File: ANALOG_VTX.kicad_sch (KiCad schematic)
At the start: 13 parts, among them U13 AT7456ELAH, U8 ZX-SH1.0-3PWT, U9 ZX-SH1.0-4PWT, Y2 XL2EL89COI-111YLC-27M

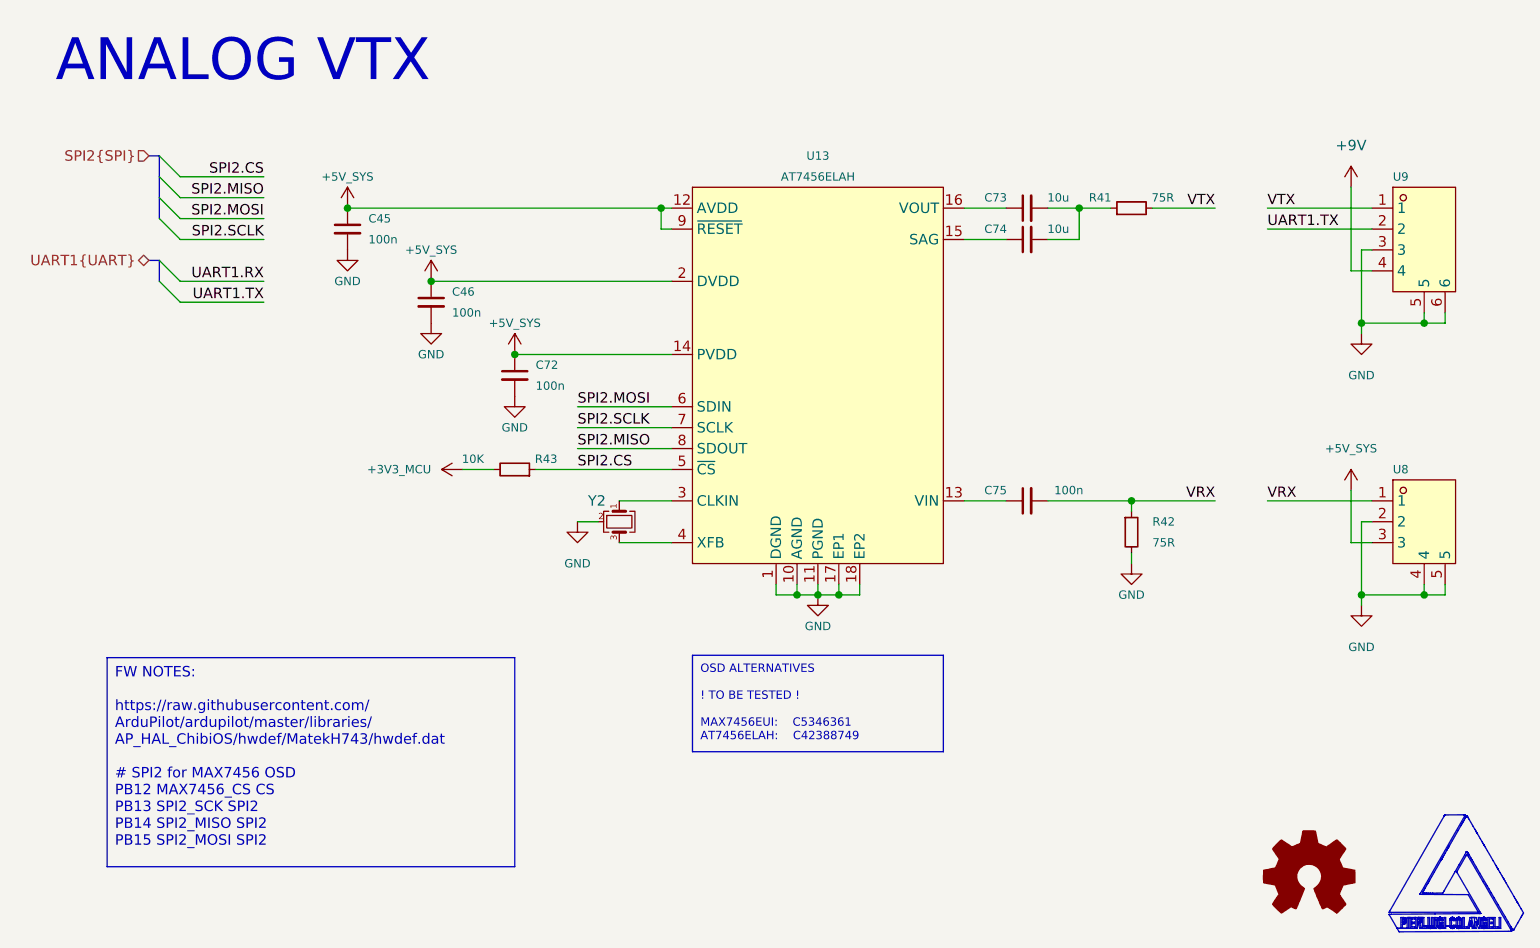
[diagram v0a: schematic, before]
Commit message: grouped ICs and passives
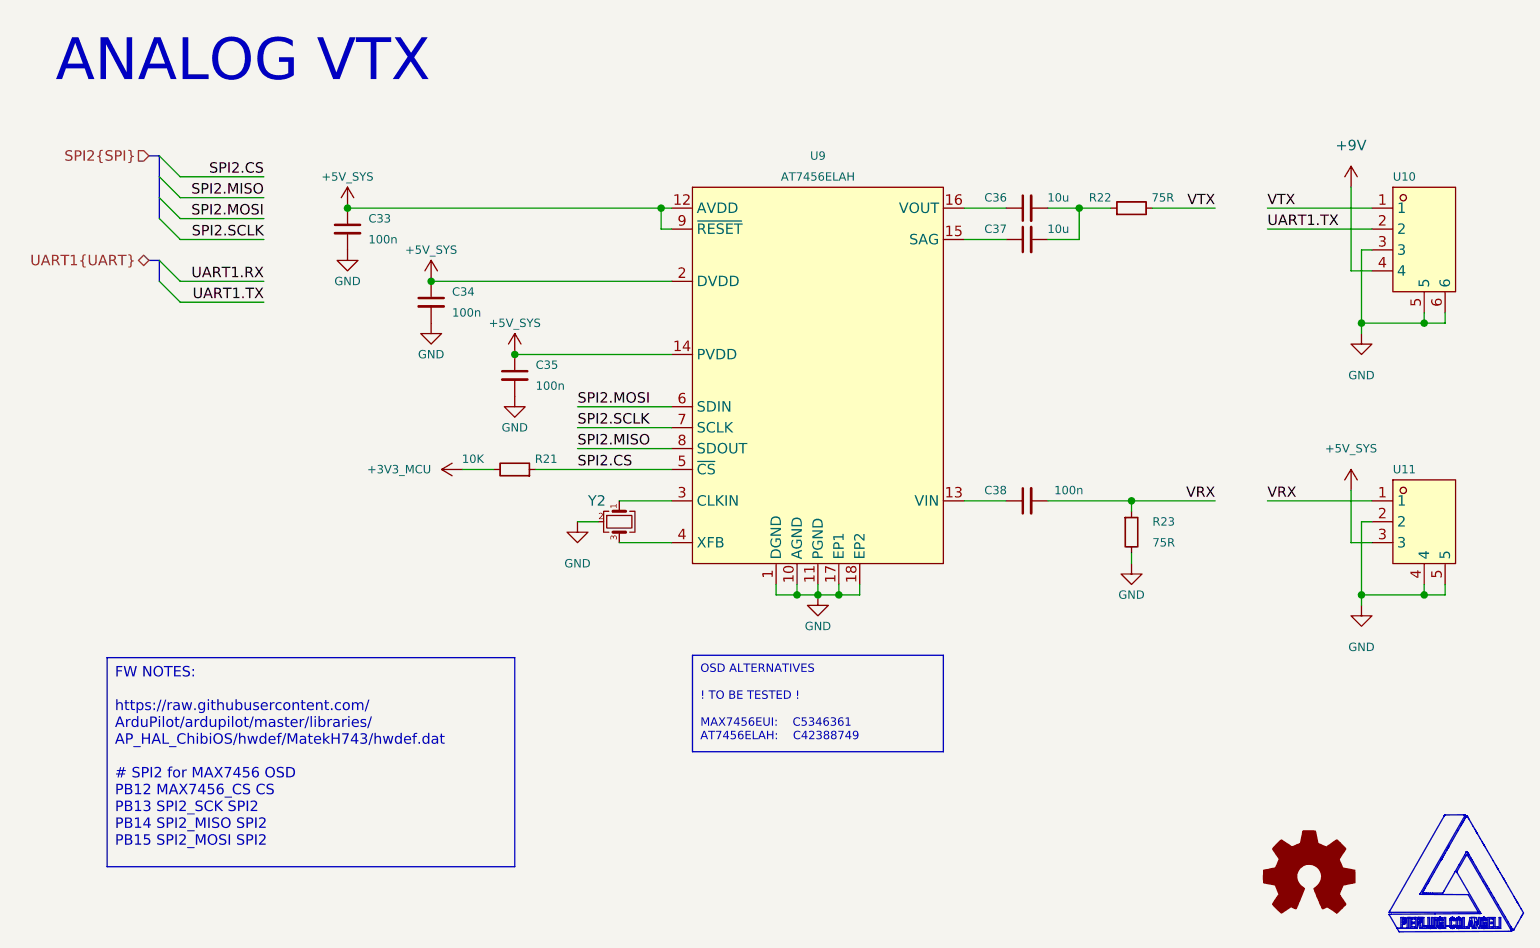
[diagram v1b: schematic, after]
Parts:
- renumbered C45 to C33, C46 to C34, C72 to C35, C73 to C36, C74 to C37, C75 to C38, R43 to R21, R41 to R22, R42 to R23, U9 to U10, U8 to U11, U13 to U9
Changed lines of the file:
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@@
 		(in_pos_files yes)
 		(dnp no)
-		(property "Reference" "#PWR0101"
+		(property "Reference" "#PWR074"
 			(at 73.66 66.04 0)
 			(hide yes)
@@
 			(project "LEVIA_H7"
 				(path "/6b768b36-fce6-4be0-9021-6d41bddc3a70/6670d797-9965-46e5-90bb-ab564d1e1d11"
-					(reference "#PWR0101")
+					(reference "#PWR074")
 					(unit 1)
 				)
@@
 		(dnp no)
 		(fields_autoplaced yes)
-		(property "Reference" "R42"
+		(property "Reference" "R23"
 			(at 151.13 74.9299 0)
 			(show_name no)
@@
 			(project "LEVIA_H7"
 				(path "/6b768b36-fce6-4be0-9021-6d41bddc3a70/6670d797-9965-46e5-90bb-ab564d1e1d11"
-					(reference "R42")
+					(reference "R23")
 					(unit 1)
 				)
@@
 		(in_pos_files yes)
 		(dnp no)
-		(property "Reference" "#PWR0100"
+		(property "Reference" "#PWR073"
 			(at 73.66 58.42 0)
 			(hide yes)
@@
 			(project "LEVIA_H7"
 				(path "/6b768b36-fce6-4be0-9021-6d41bddc3a70/6670d797-9965-46e5-90bb-ab564d1e1d11"
-					(reference "#PWR0100")
+					(reference "#PWR073")
 					(unit 1)
 				)
@@
 		(in_pos_files yes)
 		(dnp no)
-		(property "Reference" "U8"
+		(property "Reference" "U11"
 			(at 180.34 68.58 0)
 			(show_name no)
@@
 			(project "LEVIA_H7"
 				(path "/6b768b36-fce6-4be0-9021-6d41bddc3a70/6670d797-9965-46e5-90bb-ab564d1e1d11"
-					(reference "U8")
+					(reference "U11")
 					(unit 1)
 				)
@@
 		(dnp no)
 		(fields_autoplaced yes)
-		(property "Reference" "#PWR061"
+		(property "Reference" "#PWR079"
 			(at 175.26 74.93 0)
 			(hide yes)
@@
 			(project "LEVIA_H7"
 				(path "/6b768b36-fce6-4be0-9021-6d41bddc3a70/6670d797-9965-46e5-90bb-ab564d1e1d11"
-					(reference "#PWR061")
+					(reference "#PWR079")
 					(unit 1)
 				)
@@
 		(dnp no)
 		(fields_autoplaced yes)
-		(property "Reference" "#PWR059"
+		(property "Reference" "#PWR080"
 			(at 176.53 58.42 0)
 			(hide yes)
@@
 			(project "LEVIA_H7"
 				(path "/6b768b36-fce6-4be0-9021-6d41bddc3a70/6670d797-9965-46e5-90bb-ab564d1e1d11"
-					(reference "#PWR059")
+					(reference "#PWR080")
 					(unit 1)
 				)
@@
 		(in_pos_files yes)
 		(dnp no)
-		(property "Reference" "U13"
+		(property "Reference" "U9"
 			(at 110.49 30.48 0)
 			(show_name no)
@@
 			(project "LEVIA_H7"
 				(path "/6b768b36-fce6-4be0-9021-6d41bddc3a70/6670d797-9965-46e5-90bb-ab564d1e1d11"
-					(reference "U13")
+					(reference "U9")
 					(unit 1)
 				)
@@
 		(in_pos_files yes)
 		(dnp no)
-		(property "Reference" "#PWR095"
+		(property "Reference" "#PWR069"
 			(at 53.34 48.26 0)
 			(hide yes)
@@
 			(project "LEVIA_H7"
 				(path "/6b768b36-fce6-4be0-9021-6d41bddc3a70/6670d797-9965-46e5-90bb-ab564d1e1d11"
-					(reference "#PWR095")
+					(reference "#PWR069")
 					(unit 1)
 				)
@@
 		(in_pos_files yes)
 		(dnp no)
-		(property "Reference" "U9"
+		(property "Reference" "U10"
 			(at 180.34 33.02 0)
 			(show_name no)
@@
 			(project "LEVIA_H7"
 				(path "/6b768b36-fce6-4be0-9021-6d41bddc3a70/6670d797-9965-46e5-90bb-ab564d1e1d11"
-					(reference "U9")
+					(reference "U10")
 					(unit 1)
 				)
@@
 		(in_pos_files yes)
 		(dnp no)
-		(property "Reference" "C75"
+		(property "Reference" "C38"
 			(at 132.08 71.12 90)
 			(show_name no)
@@
 			(project "LEVIA_H7"
 				(path "/6b768b36-fce6-4be0-9021-6d41bddc3a70/6670d797-9965-46e5-90bb-ab564d1e1d11"
-					(reference "C75")
+					(reference "C38")
 					(unit 1)
 				)
@@
 		(dnp no)
 		(fields_autoplaced yes)
-		(property "Reference" "C46"
+		(property "Reference" "C34"
 			(at 66.04 46.9962 0)
 			(show_name no)
@@
 			(project "LEVIA_H7"
 				(path "/6b768b36-fce6-4be0-9021-6d41bddc3a70/6670d797-9965-46e5-90bb-ab564d1e1d11"
-					(reference "C46")
+					(reference "C34")
 					(unit 1)
 				)
@@
 		(in_pos_files yes)
 		(dnp no)
-		(property "Reference" "C74"
+		(property "Reference" "C37"
 			(at 132.08 39.37 90)
 			(show_name no)
@@
 			(project "LEVIA_H7"
 				(path "/6b768b36-fce6-4be0-9021-6d41bddc3a70/6670d797-9965-46e5-90bb-ab564d1e1d11"
-					(reference "C74")
+					(reference "C37")
 					(unit 1)
 				)
@@
 		(in_pos_files yes)
 		(dnp no)
-		(property "Reference" "R41"
+		(property "Reference" "R22"
 			(at 144.78 35.56 90)
 			(show_name no)
@@
 			(project "LEVIA_H7"
 				(path "/6b768b36-fce6-4be0-9021-6d41bddc3a70/6670d797-9965-46e5-90bb-ab564d1e1d11"
-					(reference "R41")
+					(reference "R22")
 					(unit 1)
 				)
@@
 		(dnp no)
 		(fields_autoplaced yes)
-		(property "Reference" "#PWR060"
+		(property "Reference" "#PWR081"
 			(at 176.53 91.44 0)
 			(hide yes)
@@
 			(project "LEVIA_H7"
 				(path "/6b768b36-fce6-4be0-9021-6d41bddc3a70/6670d797-9965-46e5-90bb-ab564d1e1d11"
-					(reference "#PWR060")
+					(reference "#PWR081")
 					(unit 1)
 				)
@@
 		(dnp no)
 		(fields_autoplaced yes)
-		(property "Reference" "C45"
+		(property "Reference" "C33"
 			(at 55.88 38.1062 0)
 			(show_name no)
@@
 			(project "LEVIA_H7"
 				(path "/6b768b36-fce6-4be0-9021-6d41bddc3a70/6670d797-9965-46e5-90bb-ab564d1e1d11"
-					(reference "C45")
+					(reference "C33")
 					(unit 1)
 				)
@@
 		(in_pos_files yes)
 		(dnp no)
-		(property "Reference" "#PWR0102"
+		(property "Reference" "#PWR076"
 			(at 110.49 90.17 0)
 			(hide yes)
@@
 			(project "LEVIA_H7"
 				(path "/6b768b36-fce6-4be0-9021-6d41bddc3a70/6670d797-9965-46e5-90bb-ab564d1e1d11"
-					(reference "#PWR0102")
+					(reference "#PWR076")
 					(unit 1)
 				)
@@
 		(in_pos_files yes)
 		(dnp no)
-		(property "Reference" "#PWR0149"
+		(property "Reference" "#PWR077"
 			(at 148.59 86.36 0)
 			(hide yes)
@@
 			(project "LEVIA_H7"
 				(path "/6b768b36-fce6-4be0-9021-6d41bddc3a70/6670d797-9965-46e5-90bb-ab564d1e1d11"
-					(reference "#PWR0149")
+					(reference "#PWR077")
 					(unit 1)
 				)
@@
 		(dnp no)
 		(fields_autoplaced yes)
-		(property "Reference" "#PWR03"
+		(property "Reference" "#PWR078"
 			(at 175.26 38.1 0)
 			(hide yes)
@@
 			(project "LEVIA_H7"
 				(path "/6b768b36-fce6-4be0-9021-6d41bddc3a70/6670d797-9965-46e5-90bb-ab564d1e1d11"
-					(reference "#PWR03")
+					(reference "#PWR078")
 					(unit 1)
 				)
@@
 		(in_pos_files yes)
 		(dnp no)
-		(property "Reference" "#PWR096"
+		(property "Reference" "#PWR070"
 			(at 63.5 49.53 0)
 			(hide yes)
@@
 			(project "LEVIA_H7"
 				(path "/6b768b36-fce6-4be0-9021-6d41bddc3a70/6670d797-9965-46e5-90bb-ab564d1e1d11"
-					(reference "#PWR096")
+					(reference "#PWR070")
 					(unit 1)
 				)
@@
 		(dnp no)
 		(fields_autoplaced yes)
-		(property "Reference" "C72"
+		(property "Reference" "C35"
 			(at 76.2 55.8862 0)
 			(show_name no)
@@
 			(project "LEVIA_H7"
 				(path "/6b768b36-fce6-4be0-9021-6d41bddc3a70/6670d797-9965-46e5-90bb-ab564d1e1d11"
-					(reference "C72")
+					(reference "C35")
 					(unit 1)
 				)
@@
 		(in_pos_files yes)
 		(dnp no)
-		(property "Reference" "#PWR0103"
+		(property "Reference" "#PWR075"
 			(at 81.28 81.28 0)
 			(hide yes)
@@
 			(project "LEVIA_H7"
 				(path "/6b768b36-fce6-4be0-9021-6d41bddc3a70/6670d797-9965-46e5-90bb-ab564d1e1d11"
-					(reference "#PWR0103")
+					(reference "#PWR075")
 					(unit 1)
 				)
@@
 		(in_pos_files yes)
 		(dnp no)
-		(property "Reference" "#PWR099"
+		(property "Reference" "#PWR071"
 			(at 63.5 57.15 0)
 			(hide yes)
@@
 			(project "LEVIA_H7"
 				(path "/6b768b36-fce6-4be0-9021-6d41bddc3a70/6670d797-9965-46e5-90bb-ab564d1e1d11"
-					(reference "#PWR099")
+					(reference "#PWR071")
 					(unit 1)
 				)
@@
 		(in_pos_files yes)
 		(dnp no)
-		(property "Reference" "C73"
+		(property "Reference" "C36"
 			(at 132.08 35.56 90)
 			(show_name no)
@@
 			(project "LEVIA_H7"
 				(path "/6b768b36-fce6-4be0-9021-6d41bddc3a70/6670d797-9965-46e5-90bb-ab564d1e1d11"
-					(reference "C73")
+					(reference "C36")
 					(unit 1)
 				)
@@
 		(in_pos_files yes)
 		(dnp no)
-		(property "Reference" "R43"
+		(property "Reference" "R21"
 			(at 77.47 67.31 90)
 			(show_name no)
@@
 			(project "LEVIA_H7"
 				(path "/6b768b36-fce6-4be0-9021-6d41bddc3a70/6670d797-9965-46e5-90bb-ab564d1e1d11"
-					(reference "R43")
+					(reference "R21")
 					(unit 1)
 				)
@@
 		(in_pos_files yes)
 		(dnp no)
-		(property "Reference" "#PWR093"
+		(property "Reference" "#PWR068"
 			(at 53.34 40.64 0)
 			(hide yes)
@@
 			(project "LEVIA_H7"
 				(path "/6b768b36-fce6-4be0-9021-6d41bddc3a70/6670d797-9965-46e5-90bb-ab564d1e1d11"
-					(reference "#PWR093")
+					(reference "#PWR068")
 					(unit 1)
 				)
@@
 		(dnp no)
 		(fields_autoplaced yes)
-		(property "Reference" "#PWR0150"
+		(property "Reference" "#PWR072"
 			(at 71.12 68.58 0)
 			(hide yes)
@@
 			(project "LEVIA_H7"
 				(path "/6b768b36-fce6-4be0-9021-6d41bddc3a70/6670d797-9965-46e5-90bb-ab564d1e1d11"
-					(reference "#PWR0150")
-					(unit 1)
-				)
+					(reference "#PWR072")
+					(unit 1)
+				)
